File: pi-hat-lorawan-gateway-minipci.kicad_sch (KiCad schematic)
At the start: 6 parts, among them Con1 RPi-Header-2x13, U1 LD39200

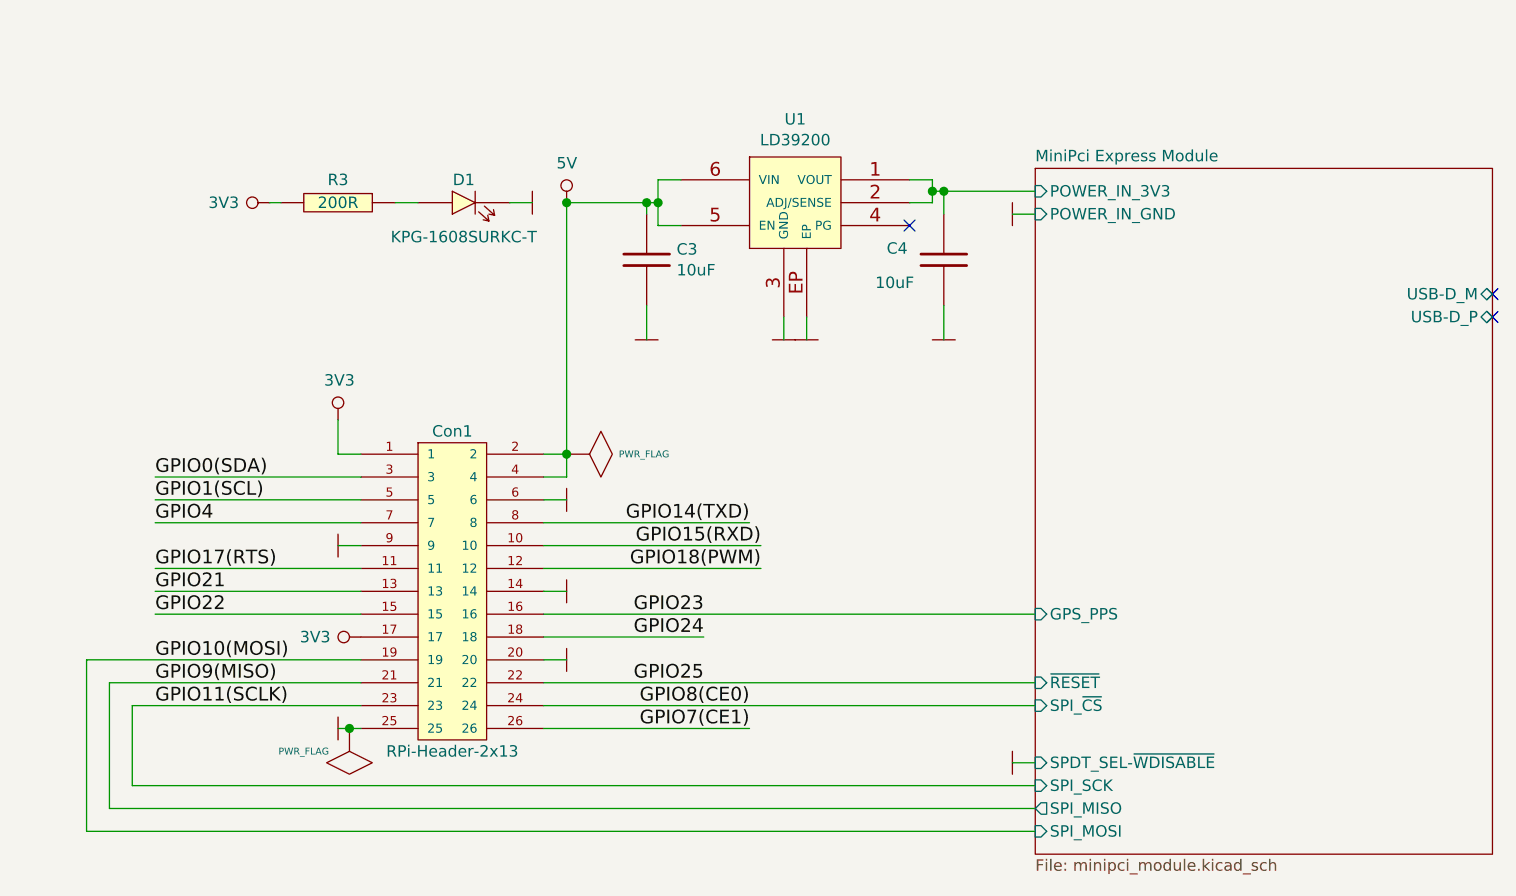
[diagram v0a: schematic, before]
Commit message: Board revorked to RPI-4 Hat Vertical
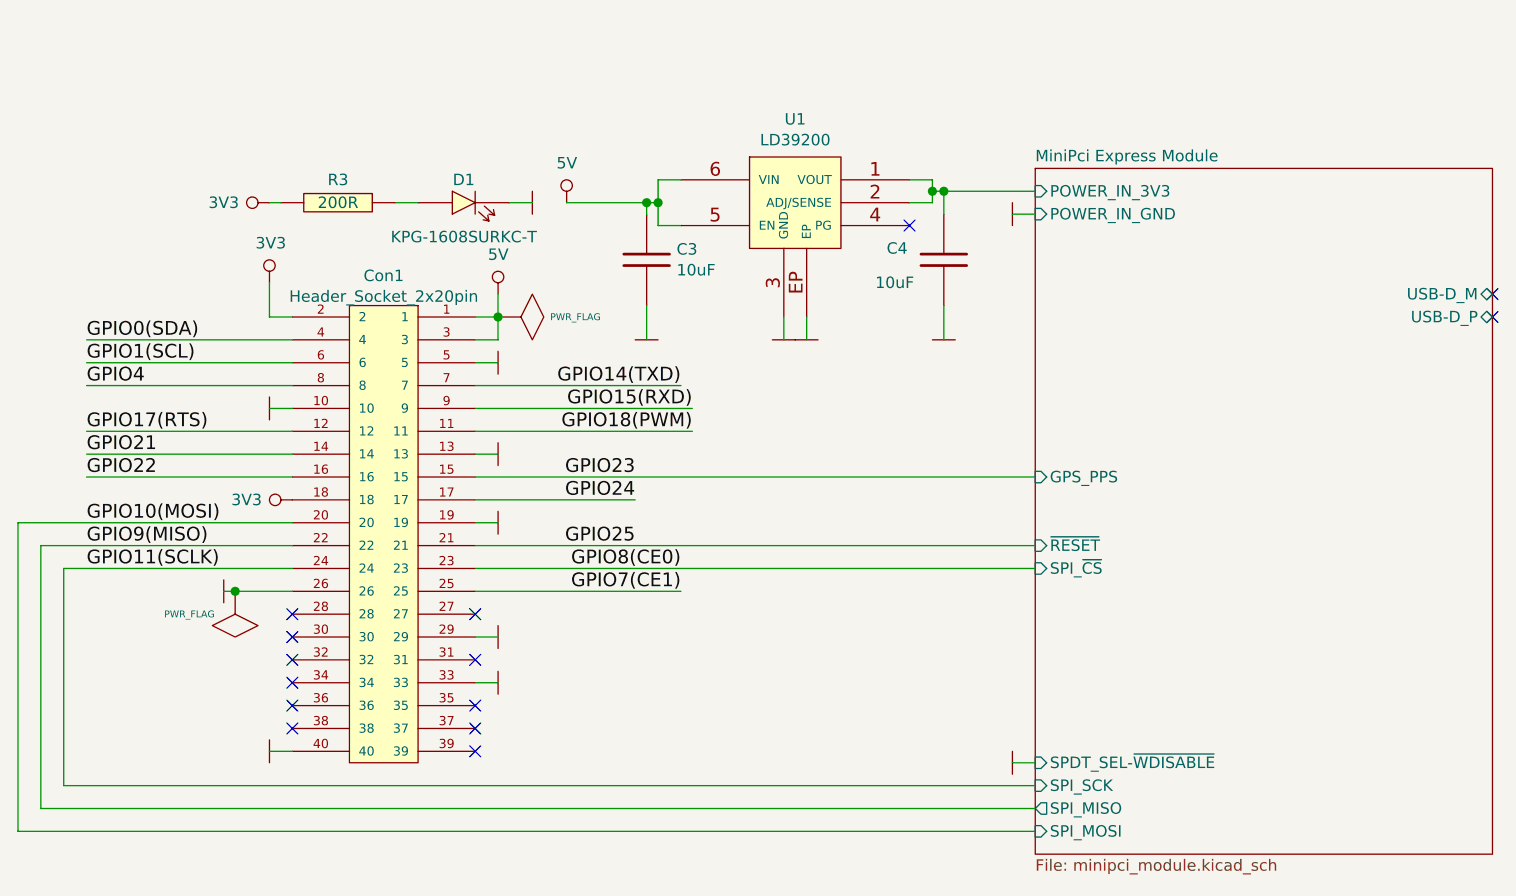
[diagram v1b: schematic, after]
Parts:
- removed Con1: RPi-Header-2x13, Header_Socket_2_54mm:Header_Socket_2x13x2_54mm, symbol Header_Socket_2_54mm:Header_Socket_2x13pin
- added Con1: Header_Socket_2x20pin, Header_Socket_2_54mm:Header_Socket_Vertical_2x20x2_54mm, symbol Header_Socket_2_54mm:Header_Socket_2x20pin
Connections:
- net 3V3: now also Con1.18, Con1.2
- net 5V: now also Con1.1, Con1.3
- net GND: now also Con1.10, Con1.13, Con1.19, Con1.26, Con1.29, Con1.33, Con1.40, Con1.5
- net GPIO0(SDA): now also Con1.4
- net GPIO1(SCL): now also Con1.6
- net GPIO10(MOSI): now also Con1.20
- net GPIO11(SCLK): now also Con1.24
- net GPIO14(TXD): now also Con1.7
- net GPIO15(RXD): now also Con1.9
- net GPIO17(RTS): now also Con1.12
- net GPIO18(PWM): now also Con1.11
- net GPIO21: now also Con1.14
- net GPIO22: now also Con1.16
- net GPIO23: now also Con1.15
- net GPIO24: now also Con1.17
- net GPIO25: now also Con1.21
- net GPIO4: now also Con1.8
- net GPIO7(CE1): now also Con1.25
- net GPIO8(CE0): now also Con1.23
- net GPIO9(MISO): now also Con1.22
- no-connect marks 3 -> 14

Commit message: Applied issue and regenerated gerbers
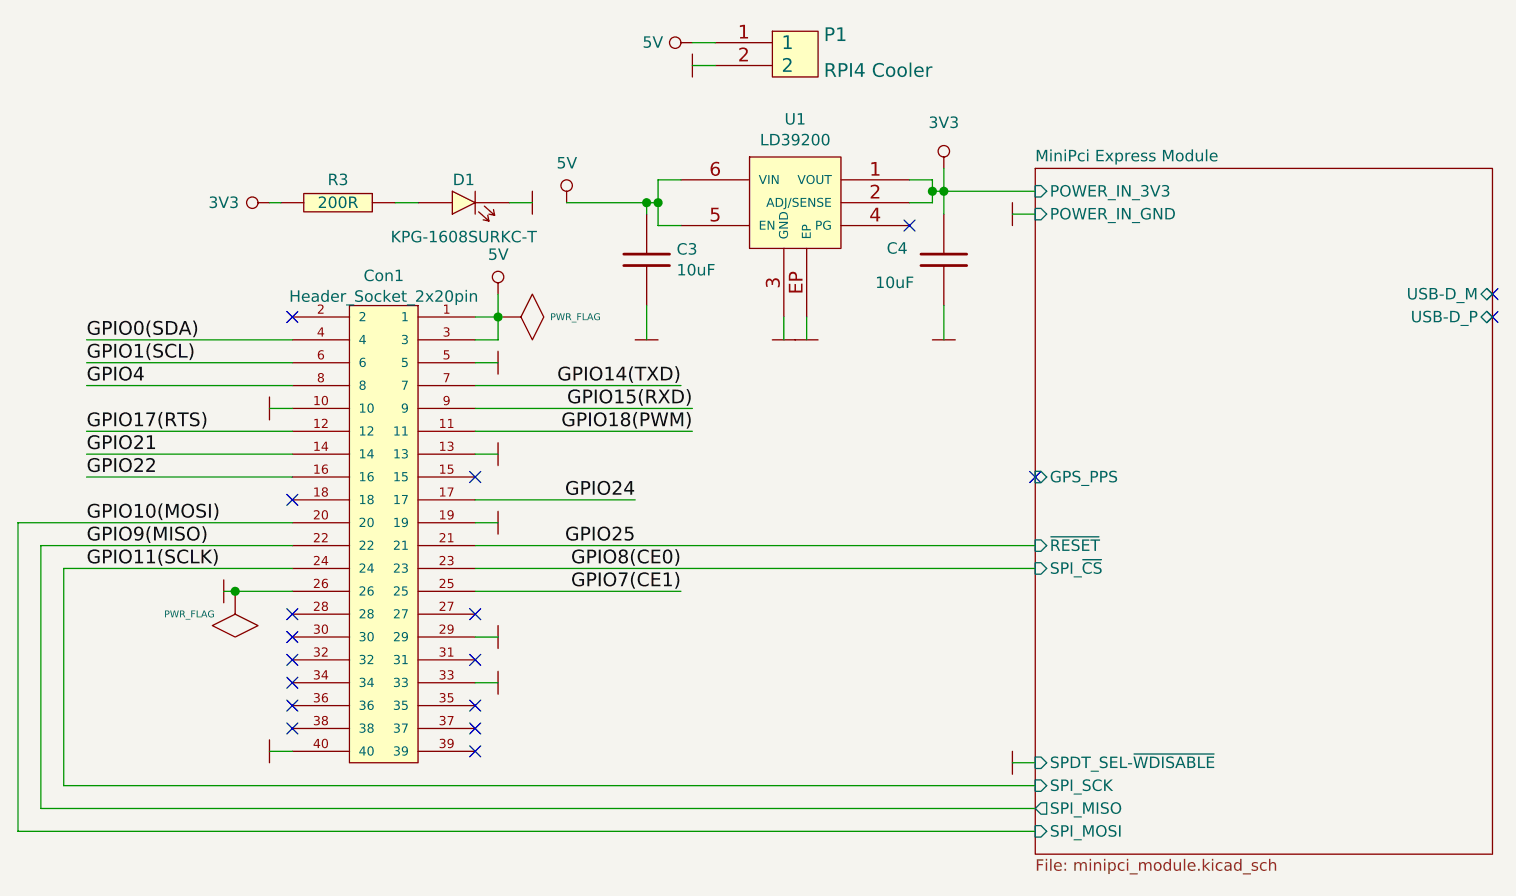
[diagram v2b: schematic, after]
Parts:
- added P1: RPI4 Cooler, Goldpin:Goldpin_2_2_54mm_90deg, symbol Goldpin_2_54mm:GOLDPIN_2_2_54MM_90DEG
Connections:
- net MiniPci Express Module/POWER_IN_3V3 is gone; now on net 3V3: C4.1, U1.1 (VOUT), U1.2 (ADJ/SENSE)
- net 3V3: no longer Con1.18, Con1.2
- net 5V: now also P1.1
- net GND: now also P1.2
- net GPIO23: no longer names the net of Con1.15
- no-connect marks 14 -> 18
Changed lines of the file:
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@@
   (junction (at 224.79 123.19) (diameter 1.016) (color 0 0 0 0))
   (junction (at 226.06 123.19) (diameter 1.016) (color 0 0 0 0))
+  (no_connect (at 153.67 137.16))
+  (no_connect (at 153.67 157.48))
   (no_connect (at 153.67 170.18))
   (no_connect (at 153.67 172.72))
@@
   (no_connect (at 153.67 180.34))
   (no_connect (at 153.67 182.88))
+  (no_connect (at 173.99 154.94))
   (no_connect (at 173.99 170.18))
   (no_connect (at 173.99 175.26))
@@
   (no_connect (at 173.99 185.42))
   (no_connect (at 222.25 127))
+  (no_connect (at 236.22 154.94))
   (no_connect (at 287.02 134.62))
   (no_connect (at 287.02 137.16))
@@
     (stroke (width 0) (type solid) (color 0 0 0 0))
   )
-  (wire (pts (xy 151.13 133.35) (xy 151.13 137.16))
-    (stroke (width 0) (type solid) (color 0 0 0 0))
-  )
-  (wire (pts (xy 151.13 137.16) (xy 153.67 137.16))
-    (stroke (width 0) (type solid) (color 0 0 0 0))
-  )
   (wire (pts (xy 151.13 147.32) (xy 153.67 147.32))
     (stroke (width 0) (type solid) (color 0 0 0 0))
@@
     (stroke (width 0) (type solid) (color 0 0 0 0))
   )
-  (wire (pts (xy 173.99 154.94) (xy 236.22 154.94))
-    (stroke (width 0) (type solid) (color 0 0 0 0))
-  )
   (wire (pts (xy 173.99 157.48) (xy 191.77 157.48))
     (stroke (width 0) (type solid) (color 0 0 0 0))
@@
     (stroke (width 0) (type solid) (color 0 0 0 0))
   )
+  (wire (pts (xy 198.12 106.68) (xy 200.66 106.68))
+    (stroke (width 0) (type solid) (color 0 0 0 0))
+  )
+  (wire (pts (xy 198.12 109.22) (xy 200.66 109.22))
+    (stroke (width 0) (type solid) (color 0 0 0 0))
+  )
   (wire (pts (xy 208.28 139.7) (xy 208.28 137.16))
     (stroke (width 0) (type solid) (color 0 0 0 0))
@@
   )
   (wire (pts (xy 224.79 124.46) (xy 224.79 123.19))
+    (stroke (width 0) (type solid) (color 0 0 0 0))
+  )
+  (wire (pts (xy 226.06 120.65) (xy 226.06 123.19))
     (stroke (width 0) (type solid) (color 0 0 0 0))
   )
@@
     (effects (font (size 1.524 1.524)) (justify left bottom))
   )
-  (label "GPIO23" (at 191.77 154.94 180)
-    (effects (font (size 1.524 1.524)) (justify right bottom))
-  )
   (label "GPIO24" (at 191.77 157.48 180)
     (effects (font (size 1.524 1.524)) (justify right bottom))
@@
     (pin "1")
   )
+  (symbol (lib_id "power:GND") (at 198.12 109.22 270) (unit 1)
+    (in_bom yes) (on_board yes)
+    (property "Reference" "#PWR0121" (id 0) (at 200.66 109.22 0)
+      (effects (font (size 0.762 0.762)) hide)
+    )
+    (property "Value" "GND" (id 1) (at 195.58 109.22 0)
+      (effects (font (size 0.762 0.762)) hide)
+    )
+    (property "Footprint" "" (id 2) (at 198.12 109.22 0)
+      (effects (font (size 1.524 1.524)))
+    )
+    (property "Datasheet" "" (id 3) (at 198.12 109.22 0)
+      (effects (font (size 1.524 1.524)))
+    )
+    (pin "1")
+  )
   (symbol (lib_id "power:GND") (at 208.28 139.7 0) (unit 1)
     (in_bom yes) (on_board yes)
@@
     (pin "1")
   )
-  (symbol (lib_id "power:3V3") (at 151.13 133.35 0) (unit 1)
-    (in_bom yes) (on_board yes)
-    (property "Reference" "#PWR01" (id 0) (at 151.13 130.81 0)
-      (effects (font (size 1.016 1.016)) hide)
-    )
-    (property "Value" "3V3" (id 1) (at 151.2824 128.9558 0))
-    (property "Footprint" "" (id 2) (at 151.13 133.35 0)
-      (effects (font (size 1.524 1.524)))
-    )
-    (property "Datasheet" "" (id 3) (at 151.13 133.35 0)
-      (effects (font (size 1.524 1.524)))
-    )
-    (pin "1")
-  )
-  (symbol (lib_id "power:3V3") (at 153.67 157.48 90) (unit 1)
-    (in_bom yes) (on_board yes)
-    (property "Reference" "#PWR0103" (id 0) (at 151.13 157.48 0)
-      (effects (font (size 1.016 1.016)) hide)
-    )
-    (property "Value" "3V3" (id 1) (at 148.59 157.48 90))
-    (property "Footprint" "" (id 2) (at 153.67 157.48 0)
-      (effects (font (size 1.524 1.524)))
-    )
-    (property "Datasheet" "" (id 3) (at 153.67 157.48 0)
-      (effects (font (size 1.524 1.524)))
-    )
-    (pin "1")
-  )
   (symbol (lib_id "power:5V") (at 176.53 134.62 0) (unit 1)
     (in_bom yes) (on_board yes)
@@
     )
     (property "Datasheet" "" (id 3) (at 184.15 124.46 0)
+      (effects (font (size 1.524 1.524)))
+    )
+    (pin "1")
+  )
+  (symbol (lib_id "power:5V") (at 198.12 106.68 90) (unit 1)
+    (in_bom yes) (on_board yes)
+    (property "Reference" "#PWR0120" (id 0) (at 198.12 107.95 90)
+      (effects (font (size 0.508 0.508)) hide)
+    )
+    (property "Value" "5V" (id 1) (at 193.7258 106.6546 90))
+    (property "Footprint" "" (id 2) (at 198.12 106.68 0)
+      (effects (font (size 1.524 1.524)))
+    )
+    (property "Datasheet" "" (id 3) (at 198.12 106.68 0)
+      (effects (font (size 1.524 1.524)))
+    )
+    (pin "1")
+  )
+  (symbol (lib_id "power:3V3") (at 226.06 120.65 0) (unit 1)
+    (in_bom yes) (on_board yes)
+    (property "Reference" "#PWR0103" (id 0) (at 226.06 118.11 0)
+      (effects (font (size 1.016 1.016)) hide)
+    )
+    (property "Value" "3V3" (id 1) (at 226.06 115.57 0))
+    (property "Footprint" "" (id 2) (at 226.06 120.65 0)
+      (effects (font (size 1.524 1.524)))
+    )
+    (property "Datasheet" "" (id 3) (at 226.06 120.65 0)
       (effects (font (size 1.524 1.524)))
     )
@@
     (property "LCSC Part # (optional)" "C162265" (id 13) (at 226.06 130.81 0)
       (effects (font (size 1.27 1.27)) hide)
+    )
+    (pin "1")
+    (pin "2")
+  )
+  (symbol (lib_id "Goldpin_2_54mm:GOLDPIN_2_2_54MM_90DEG") (at 209.55 107.95 0) (unit 1)
+    (in_bom yes) (on_board yes)
+    (property "Reference" "P1" (id 0) (at 212.7251 105.7924 0)
+      (effects (font (size 1.524 1.524)) (justify left))
+    )
+    (property "Value" "RPI4 Cooler" (id 1) (at 212.7251 109.77 0)
+      (effects (font (size 1.524 1.524)) (justify left))
+    )
+    (property "Footprint" "Goldpin:Goldpin_2_2_54mm_90deg" (id 2) (at 242.57 92.71 0)
+      (effects (font (size 1.524 1.524)) hide)
+    )
+    (property "Datasheet" "Goldpins/Components_Documentation/Goldpin_2_54mm.pdf" (id 3) (at 212.7251 111.1238 0)
+      (effects (font (size 1.524 1.524)) (justify left) hide)
     )
     (pin "1")
@@
       (reference "#FLG0103") (unit 1) (value "PWR_FLAG") (footprint "")
     )
-    (path "/00000000-0000-0000-0000-00006009ec17"
-      (reference "#PWR01") (unit 1) (value "3V3") (footprint "")
-    )
     (path "/00000000-0000-0000-0000-00006009e70a"
       (reference "#PWR02") (unit 1) (value "5V") (footprint "")
@@
       (reference "#PWR0102") (unit 1) (value "GND") (footprint "")
     )
-    (path "/00000000-0000-0000-0000-0000600a0e97"
+    (path "/0e64aa89-df79-4f3c-a2c2-2d8fd6e31690"
       (reference "#PWR0103") (unit 1) (value "3V3") (footprint "")
     )
@@
       (reference "#PWR0119") (unit 1) (value "5V") (footprint "")
     )
+    (path "/01a74e1e-c3eb-42b1-ac7f-0d504a0b6d12"
+      (reference "#PWR0120") (unit 1) (value "5V") (footprint "")
+    )
+    (path "/8b04b3b7-5cc1-4efe-b512-fe2b1f83e509"
+      (reference "#PWR0121") (unit 1) (value "GND") (footprint "")
+    )
     (path "/00000000-0000-0000-0000-0000600be1b9"
       (reference "C3") (unit 1) (value "10uF") (footprint "Capacitors_Smd_0603:10uF_10V_0603")
@@
       (reference "D1") (unit 1) (value "KPG-1608SURKC-T") (footprint "Diodes:LED_KPG-1608SURKC-T")
     )
+    (path "/9b21150f-09bd-4bfb-828e-a608ab6a5013"
+      (reference "P1") (unit 1) (value "RPI4 Cooler") (footprint "Goldpin:Goldpin_2_2_54mm_90deg")
+    )
     (path "/00000000-0000-0000-0000-0000600d2133"
       (reference "R3") (unit 1) (value "200R") (footprint "Resistor_Smd_0603:200R_0603")
@@
       (reference "#PWR010") (unit 1) (value "GND") (footprint "")
     )
-    (path "/00000000-0000-0000-0000-0000600a248e/00000000-0000-0000-0000-0000600a2e53"
-      (reference "#PWR011") (unit 1) (value "GND") (footprint "")
-    )
     (path "/00000000-0000-0000-0000-0000600a248e/00000000-0000-0000-0000-00006009c5ab"
